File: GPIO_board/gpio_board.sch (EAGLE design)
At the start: 17 parts, among them J1 SWITCHES, J2 LED1, J3 LED2, Q1 IRF520, Q2 IRF520, Q3 IRF520, X1 PCI-E-164SLOT

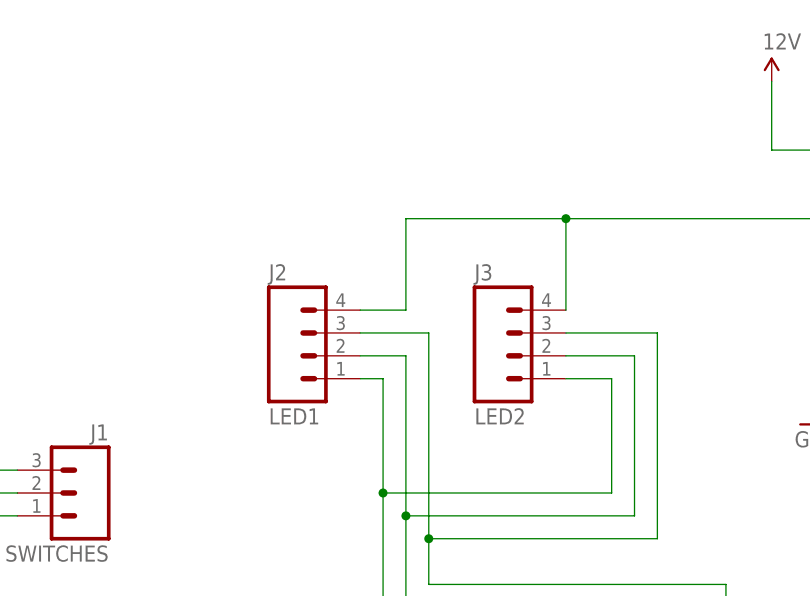
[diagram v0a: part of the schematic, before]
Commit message: added breakout pads for RGB LED drivers
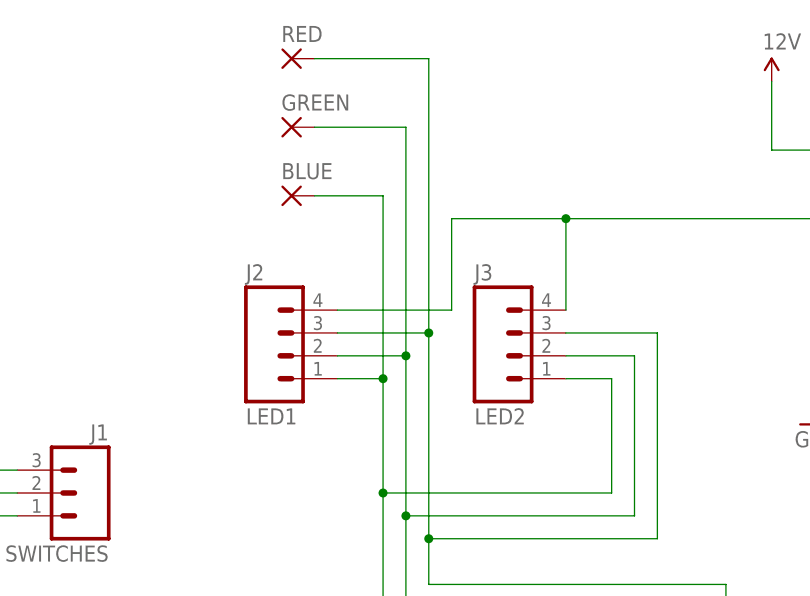
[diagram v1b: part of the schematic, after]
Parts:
- added BLUE, GREEN, RED: (no value), wirepad:2,54/1,0
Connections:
- removed net N$4: J2.1, J3.1, Q1.D
- new net N$47: BLUE.P, J2.1, J3.1, Q1.D
- net N$10: now also RED.P
- net N$6: now also GREEN.P
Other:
- moved on the sheet: J2
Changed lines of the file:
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@@
 <part name="J4" library="SparkFun-Connectors" deviceset="M02" device="PTH"/>
 <part name="J5" library="SparkFun-Connectors" deviceset="M02" device="PTH"/>
+<part name="BLUE" library="wirepad" deviceset="2,54/1,0" device=""/>
+<part name="GREEN" library="wirepad" deviceset="2,54/1,0" device=""/>
+<part name="RED" library="wirepad" deviceset="2,54/1,0" device=""/>
 </parts>
 <sheets>
@@
 <instance part="U$1" gate="G$1" x="96.52" y="106.68" rot="MR0"/>
 <instance part="J1" gate="J$1" x="147.32" y="154.94" rot="MR0"/>
-<instance part="J2" gate="G$1" x="172.72" y="170.18"/>
+<instance part="J2" gate="G$1" x="170.18" y="170.18"/>
 <instance part="J3" gate="G$1" x="195.58" y="170.18"/>
 <instance part="GND1" gate="1" x="134.62" y="142.24"/>
@@
 <instance part="J4" gate="G$1" x="101.6" y="149.86"/>
 <instance part="J5" gate="G$1" x="53.34" y="129.54"/>
+<instance part="BLUE" gate="P" x="170.18" y="187.96"/>
+<instance part="GREEN" gate="P" x="170.18" y="195.58"/>
+<instance part="RED" gate="P" x="170.18" y="203.2"/>
 </instances>
 <busses>
@@
 </segment>
 </net>
-<net name="N$4" class="0">
-<segment>
-<pinref part="J2" gate="G$1" pin="1"/>
-<pinref part="Q1" gate="G$1" pin="D"/>
-<wire x1="177.8" y1="167.64" x2="180.34" y2="167.64" width="0.1524" layer="91"/>
-<wire x1="180.34" y1="167.64" x2="180.34" y2="154.94" width="0.1524" layer="91"/>
-<pinref part="J3" gate="G$1" pin="1"/>
-<wire x1="180.34" y1="154.94" x2="180.34" y2="139.7" width="0.1524" layer="91"/>
-<wire x1="200.66" y1="167.64" x2="205.74" y2="167.64" width="0.1524" layer="91"/>
-<wire x1="205.74" y1="167.64" x2="205.74" y2="154.94" width="0.1524" layer="91"/>
-<wire x1="205.74" y1="154.94" x2="180.34" y2="154.94" width="0.1524" layer="91"/>
-<junction x="180.34" y="154.94"/>
-</segment>
-</net>
 <net name="N$6" class="0">
 <segment>
 <pinref part="J2" gate="G$1" pin="2"/>
-<wire x1="177.8" y1="170.18" x2="182.88" y2="170.18" width="0.1524" layer="91"/>
+<wire x1="175.26" y1="170.18" x2="182.88" y2="170.18" width="0.1524" layer="91"/>
 <wire x1="182.88" y1="170.18" x2="182.88" y2="152.4" width="0.1524" layer="91"/>
 <pinref part="Q2" gate="G$1" pin="D"/>
@@
 <wire x1="208.28" y1="152.4" x2="182.88" y2="152.4" width="0.1524" layer="91"/>
 <junction x="182.88" y="152.4"/>
+<pinref part="GREEN" gate="P" pin="P"/>
+<wire x1="172.72" y1="195.58" x2="182.88" y2="195.58" width="0.1524" layer="91"/>
+<wire x1="182.88" y1="195.58" x2="182.88" y2="170.18" width="0.1524" layer="91"/>
+<junction x="182.88" y="170.18"/>
 </segment>
 </net>
@@
 <wire x1="210.82" y1="172.72" x2="210.82" y2="149.86" width="0.1524" layer="91"/>
 <pinref part="J2" gate="G$1" pin="3"/>
-<wire x1="177.8" y1="172.72" x2="185.42" y2="172.72" width="0.1524" layer="91"/>
+<wire x1="175.26" y1="172.72" x2="185.42" y2="172.72" width="0.1524" layer="91"/>
 <wire x1="185.42" y1="172.72" x2="185.42" y2="149.86" width="0.1524" layer="91"/>
 <pinref part="Q3" gate="G$1" pin="D"/>
@@
 <wire x1="210.82" y1="149.86" x2="185.42" y2="149.86" width="0.1524" layer="91"/>
 <junction x="185.42" y="149.86"/>
+<pinref part="RED" gate="P" pin="P"/>
+<wire x1="172.72" y1="203.2" x2="185.42" y2="203.2" width="0.1524" layer="91"/>
+<wire x1="185.42" y1="203.2" x2="185.42" y2="172.72" width="0.1524" layer="91"/>
+<junction x="185.42" y="172.72"/>
 </segment>
 </net>
@@
 <junction x="228.6" y="187.96"/>
 <pinref part="J2" gate="G$1" pin="4"/>
-<wire x1="177.8" y1="175.26" x2="182.88" y2="175.26" width="0.1524" layer="91"/>
-<wire x1="182.88" y1="175.26" x2="182.88" y2="185.42" width="0.1524" layer="91"/>
-<wire x1="182.88" y1="185.42" x2="200.66" y2="185.42" width="0.1524" layer="91"/>
+<wire x1="175.26" y1="175.26" x2="187.96" y2="175.26" width="0.1524" layer="91"/>
+<wire x1="187.96" y1="175.26" x2="187.96" y2="185.42" width="0.1524" layer="91"/>
+<wire x1="187.96" y1="185.42" x2="200.66" y2="185.42" width="0.1524" layer="91"/>
 <junction x="228.6" y="185.42"/>
 <pinref part="J3" gate="G$1" pin="4"/>
@@
 </segment>
 </net>
+<net name="N$47" class="0">
+<segment>
+<pinref part="J2" gate="G$1" pin="1"/>
+<pinref part="Q1" gate="G$1" pin="D"/>
+<wire x1="175.26" y1="167.64" x2="180.34" y2="167.64" width="0.1524" layer="91"/>
+<wire x1="180.34" y1="167.64" x2="180.34" y2="154.94" width="0.1524" layer="91"/>
+<pinref part="J3" gate="G$1" pin="1"/>
+<wire x1="180.34" y1="154.94" x2="180.34" y2="139.7" width="0.1524" layer="91"/>
+<wire x1="200.66" y1="167.64" x2="205.74" y2="167.64" width="0.1524" layer="91"/>
+<wire x1="205.74" y1="167.64" x2="205.74" y2="154.94" width="0.1524" layer="91"/>
+<wire x1="205.74" y1="154.94" x2="180.34" y2="154.94" width="0.1524" layer="91"/>
+<junction x="180.34" y="154.94"/>
+<pinref part="BLUE" gate="P" pin="P"/>
+<wire x1="172.72" y1="187.96" x2="180.34" y2="187.96" width="0.1524" layer="91"/>
+<wire x1="180.34" y1="187.96" x2="180.34" y2="167.64" width="0.1524" layer="91"/>
+<junction x="180.34" y="167.64"/>
+</segment>
+</net>
